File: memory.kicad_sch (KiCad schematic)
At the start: 19 parts, among them U2 IS43TR16640C-125JBL

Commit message: DDR is hard
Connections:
- net BA0: no longer U2.M2 (BA0)
- net BA1: no longer U2.N8 (BA1)
- net BA2: no longer U2.M3 (BA2)
- new net DDR_BA0: U2.M2 (BA0)
- new net DDR_BA1: U2.N8 (BA1)
- new net DDR_BA2: U2.M3 (BA2)
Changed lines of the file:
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@@
 	)
 	(bus_entry
-		(at 38.1 24.13)
+		(at 38.1 74.93)
 		(size 2.54 2.54)
 		(stroke
@@
 	)
 	(bus_entry
-		(at 38.1 119.38)
+		(at 38.1 24.13)
 		(size 2.54 2.54)
 		(stroke
@@
 	)
 	(bus_entry
-		(at 38.1 99.06)
+		(at 38.1 119.38)
 		(size 2.54 2.54)
 		(stroke
@@
 	)
 	(bus_entry
-		(at 38.1 106.68)
+		(at 38.1 99.06)
 		(size 2.54 2.54)
 		(stroke
@@
 	)
 	(bus_entry
-		(at 38.1 59.69)
+		(at 38.1 106.68)
 		(size 2.54 2.54)
 		(stroke
@@
 	)
 	(bus_entry
-		(at 38.1 77.47)
+		(at 38.1 59.69)
 		(size 2.54 2.54)
 		(stroke
@@
 	)
 	(bus_entry
-		(at 38.1 52.07)
+		(at 38.1 69.85)
 		(size 2.54 2.54)
 		(stroke
@@
 	)
 	(bus_entry
-		(at 38.1 127)
+		(at 38.1 52.07)
 		(size 2.54 2.54)
 		(stroke
@@
 	)
 	(bus_entry
-		(at 38.1 34.29)
+		(at 38.1 127)
 		(size 2.54 2.54)
 		(stroke
@@
 	)
 	(bus_entry
-		(at 38.1 31.75)
+		(at 38.1 34.29)
 		(size 2.54 2.54)
 		(stroke
@@
 	)
 	(bus_entry
-		(at 38.1 88.9)
+		(at 38.1 31.75)
 		(size 2.54 2.54)
 		(stroke
@@
 	)
 	(bus_entry
-		(at 38.1 121.92)
+		(at 38.1 88.9)
 		(size 2.54 2.54)
 		(stroke
@@
 	)
 	(bus_entry
-		(at 38.1 72.39)
+		(at 38.1 121.92)
 		(size 2.54 2.54)
 		(stroke
@@
 	)
 	(bus_entry
-		(at 38.1 74.93)
+		(at 38.1 124.46)
 		(size 2.54 2.54)
 		(stroke
@@
 	)
 	(bus_entry
-		(at 38.1 124.46)
+		(at 38.1 41.91)
 		(size 2.54 2.54)
 		(stroke
@@
 	)
 	(bus_entry
-		(at 38.1 41.91)
+		(at 38.1 72.39)
 		(size 2.54 2.54)
 		(stroke
@@
 	(wire
 		(pts
+			(xy 40.64 72.39) (xy 50.8 72.39)
+		)
+		(stroke
+			(width 0)
+			(type default)
+		)
+	)
+	(wire
+		(pts
 			(xy 80.01 93.98) (xy 91.44 93.98)
 		)
@@
 		)
 	)
-	(wire
-		(pts
-			(xy 40.64 77.47) (xy 50.8 77.47)
-		)
-		(stroke
-			(width 0)
-			(type default)
-		)
-	)
 	(bus
 		(pts
@@
 		)
 	)
-	(bus
-		(pts
-			(xy 38.1 74.93) (xy 38.1 77.47)
-		)
-		(stroke
-			(width 0)
-			(type default)
-		)
-	)
 	(wire
 		(pts
@@
 	(wire
 		(pts
-			(xy 40.64 80.01) (xy 50.8 80.01)
-		)
-		(stroke
-			(width 0)
-			(type default)
-		)
-	)
-	(wire
-		(pts
 			(xy 80.01 30.48) (xy 91.44 30.48)
 		)
@@
 		)
 	)
-	(wire
+	(bus
 		(pts
-			(xy 142.24 30.48) (xy 156.21 30.48)
+			(xy 38.1 72.39) (xy 38.1 74.93)
 		)
 		(stroke
@@
 	(wire
 		(pts
-			(xy 40.64 96.52) (xy 50.8 96.52)
+			(xy 142.24 30.48) (xy 156.21 30.48)
 		)
 		(stroke
@@
 	(wire
 		(pts
-			(xy 142.24 99.06) (xy 156.21 99.06)
+			(xy 40.64 96.52) (xy 50.8 96.52)
 		)
 		(stroke
@@
 	(wire
 		(pts
-			(xy 142.24 40.64) (xy 146.05 40.64)
+			(xy 142.24 99.06) (xy 156.21 99.06)
 		)
 		(stroke
@@
 	(wire
 		(pts
-			(xy 40.64 74.93) (xy 50.8 74.93)
+			(xy 142.24 40.64) (xy 146.05 40.64)
 		)
 		(stroke
@@
 	(wire
 		(pts
+			(xy 40.64 74.93) (xy 50.8 74.93)
+		)
+		(stroke
+			(width 0)
+			(type default)
+		)
+	)
+	(wire
+		(pts
 			(xy 40.64 121.92) (xy 50.8 121.92)
 		)
@@
 	(bus
 		(pts
-			(xy 38.1 72.39) (xy 38.1 74.93)
+			(xy 38.1 69.85) (xy 38.1 72.39)
 		)
 		(stroke
@@
 	(wire
 		(pts
-			(xy 142.24 191.77) (xy 154.94 191.77)
+			(xy 40.64 77.47) (xy 50.8 77.47)
 		)
 		(stroke
@@
 	(wire
 		(pts
-			(xy 80.01 38.1) (xy 91.44 38.1)
+			(xy 142.24 191.77) (xy 154.94 191.77)
 		)
 		(stroke
@@
 		)
 	)
-	(bus
+	(wire
 		(pts
-			(xy 38.1 69.85) (xy 38.1 72.39)
+			(xy 80.01 38.1) (xy 91.44 38.1)
 		)
 		(stroke
@@
 		)
 	)
-	(label "BA2"
-		(at 50.8 74.93 180)
-		(fields_autoplaced yes)
-		(effects
-			(font
-				(size 1.27 1.27)
-			)
-			(justify right bottom)
-		)
-	)
 	(label "VDD"
 		(at 80.01 137.16 0)
@@
 		)
 	)
+	(label "DDR_BA1"
+		(at 50.8 74.93 180)
+		(effects
+			(font
+				(size 1.27 1.27)
+			)
+			(justify right bottom)
+		)
+	)
 	(label "A6"
 		(at 50.8 114.3 180)
@@
 		)
 	)
+	(label "DDR_BA1"
+		(at 156.21 76.2 180)
+		(fields_autoplaced yes)
+		(effects
+			(font
+				(size 1.27 1.27)
+			)
+			(justify right bottom)
+		)
+	)
 	(label "CK_N"
 		(at 142.24 191.77 0)
@@
 		)
 	)
-	(label "BA0"
-		(at 50.8 80.01 180)
-		(fields_autoplaced yes)
-		(effects
-			(font
-				(size 1.27 1.27)
-			)
-			(justify right bottom)
-		)
-	)
 	(label "A3"
 		(at 156.21 83.82 180)
@@
 		)
 	)
-	(label "VDD"
-		(at 80.01 27.94 0)
+	(label "DDR_BA2"
+		(at 156.21 96.52 180)
 		(fields_autoplaced yes)
 		(effects
@@
 				(size 1.27 1.27)
 			)
-			(justify left bottom)
+			(justify right bottom)
 		)
 	)
-	(label "BA0"
-		(at 156.21 99.06 180)
+	(label "VDD"
+		(at 80.01 27.94 0)
 		(fields_autoplaced yes)
 		(effects
@@
 				(size 1.27 1.27)
 			)
-			(justify right bottom)
+			(justify left bottom)
 		)
 	)
@@
 		)
 	)
-	(label "BA1"
-		(at 50.8 77.47 180)
-		(fields_autoplaced yes)
-		(effects
-			(font
-				(size 1.27 1.27)
-			)
-			(justify right bottom)
-		)
-	)
 	(label "VREF"
 		(at 156.21 91.44 180)
@@
 		)
 	)
+	(label "DDR_BA0"
+		(at 156.21 99.06 180)
+		(fields_autoplaced yes)
+		(effects
+			(font
+				(size 1.27 1.27)
+			)
+			(justify right bottom)
+		)
+	)
 	(label "CK_P"
 		(at 142.24 179.07 0)
@@
 		)
 	)
+	(label "DDR_BA0"
+		(at 50.8 72.39 180)
+		(effects
+			(font
+				(size 1.27 1.27)
+			)
+			(justify right bottom)
+		)
+	)
 	(label "A6"
 		(at 156.21 45.72 180)
@@
 		)
 	)
-	(label "WEn"
-		(at 156.21 111.76 180)
-		(fields_autoplaced yes)
-		(effects
-			(font
-				(size 1.27 1.27)
-			)
-			(justify right bottom)
-		)
-	)
-	(label "DQ9"
-		(at 50.8 39.37 180)
-		(fields_autoplaced yes)
+	(label "DDR_BA2"
+		(at 50.8 77.47 180)
 		(effects
 			(font
@@
 		)
 	)
-	(label "BA2"
-		(at 156.21 96.52 180)
+	(label "WEn"
+		(at 156.21 111.76 180)
 		(fields_autoplaced yes)
 		(effects
@@
 		)
 	)
-	(label "BA1"
-		(at 156.21 76.2 180)
+	(label "DQ9"
+		(at 50.8 39.37 180)
 		(fields_autoplaced yes)
 		(effects
@@
 		)
 	)
-	(hierarchical_label "RAS"
+	(hierarchical_label "DDR_BA[0..2]"
 		(shape input)
-		(at 156.21 142.24 0)
+		(at 33.02 69.85 180)
 		(fields_autoplaced yes)
 		(effects
@@
 				(size 1.27 1.27)
 			)
-			(justify left)
+			(justify right)
 		)
 	)
-	(hierarchical_label "DDR_BA[0..2]"
+	(hierarchical_label "RAS"
 		(shape input)
-		(at 33.02 69.85 180)
+		(at 156.21 142.24 0)
 		(fields_autoplaced yes)
 		(effects
@@
 				(size 1.27 1.27)
 			)
-			(justify right)
+			(justify left)
 		)
 	)

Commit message: DDR routing forever
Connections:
- net VDD: now also U2.C1 (VDDQ)
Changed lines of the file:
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@@
 	(label "DDR_BA1"
 		(at 50.8 74.93 180)
+		(fields_autoplaced yes)
 		(effects
 			(font
@@
 	(label "DDR_BA0"
 		(at 50.8 72.39 180)
+		(fields_autoplaced yes)
 		(effects
 			(font
@@
 	(label "DDR_BA2"
 		(at 50.8 77.47 180)
-		(effects
-			(font
-				(size 1.27 1.27)
-			)
-			(justify right bottom)
-		)
-	)
+		(fields_autoplaced yes)
+		(effects
+			(font
+				(size 1.27 1.27)
+			)
+			(justify right bottom)
+		)
+	)
+	(label "VDD"
+		(at 80.01 58.42 0)
+		(fields_autoplaced yes)
+		(effects
+			(font
+				(size 1.27 1.27)
+			)
+			(justify left bottom)
+		)
+	)

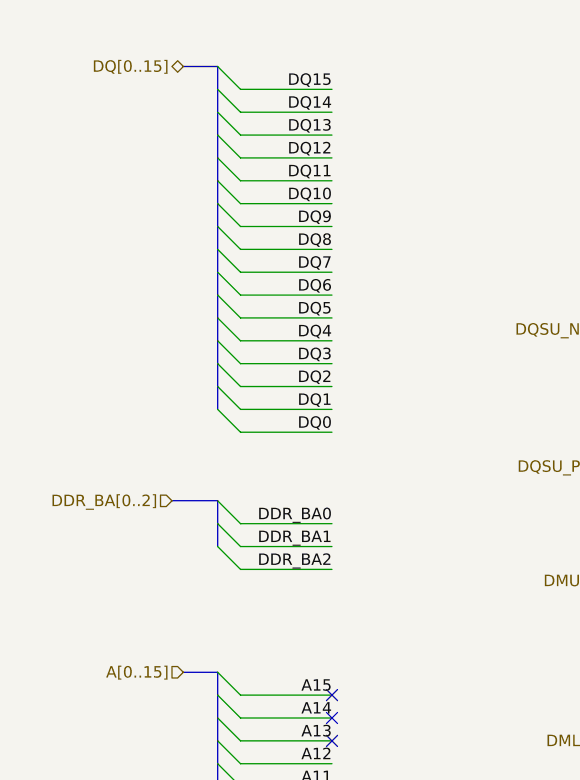
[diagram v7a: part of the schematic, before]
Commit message: DDR routing first pass complete
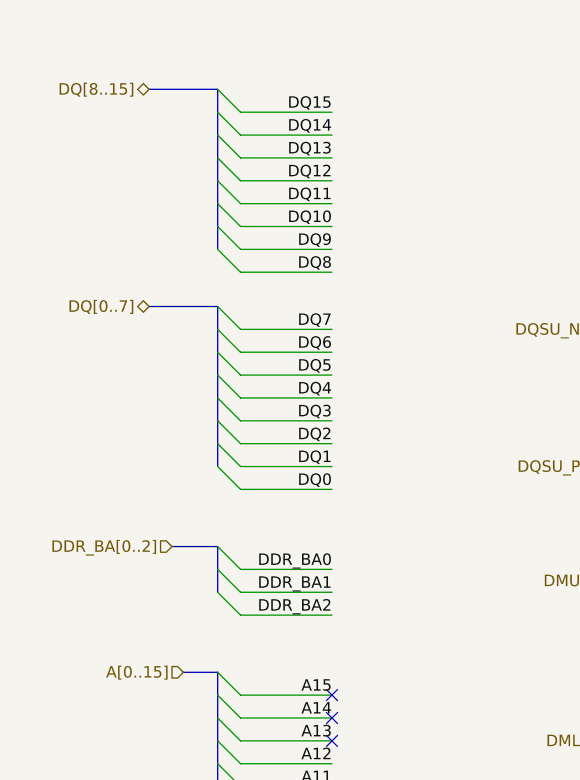
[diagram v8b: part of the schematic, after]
